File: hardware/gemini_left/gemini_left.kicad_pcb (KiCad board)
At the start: 2 copper layers, 39 parts, among them IC1 XL9555__TSSOP-24_, J1 USB_C_Receptacle_USB2.0_16P, SW1 SW_Push, SW10 SW_Push, SW11 SW_Push, SW12 SW_Push, SW13 SW_Push, SW14 SW_Push, SW15 SW_Push, SW16 SW_Push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

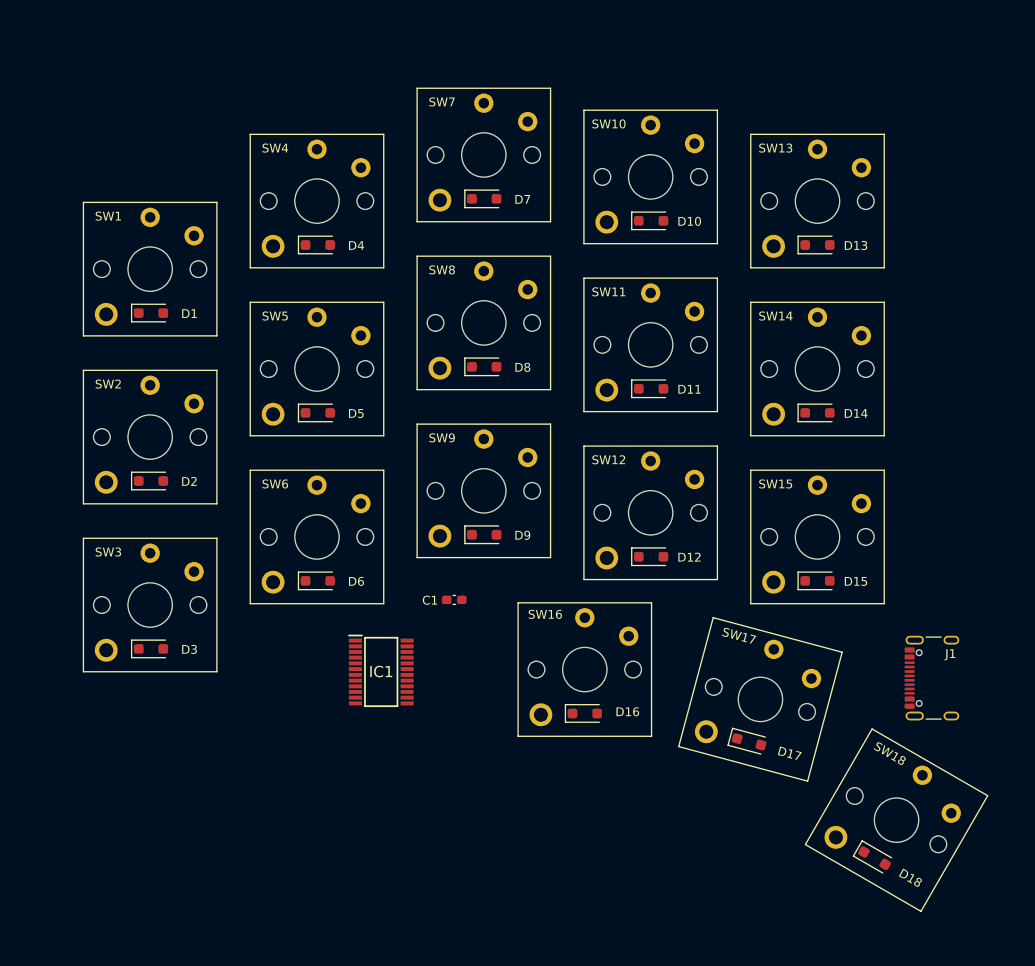
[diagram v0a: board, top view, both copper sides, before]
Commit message: routing of left side & cleanup
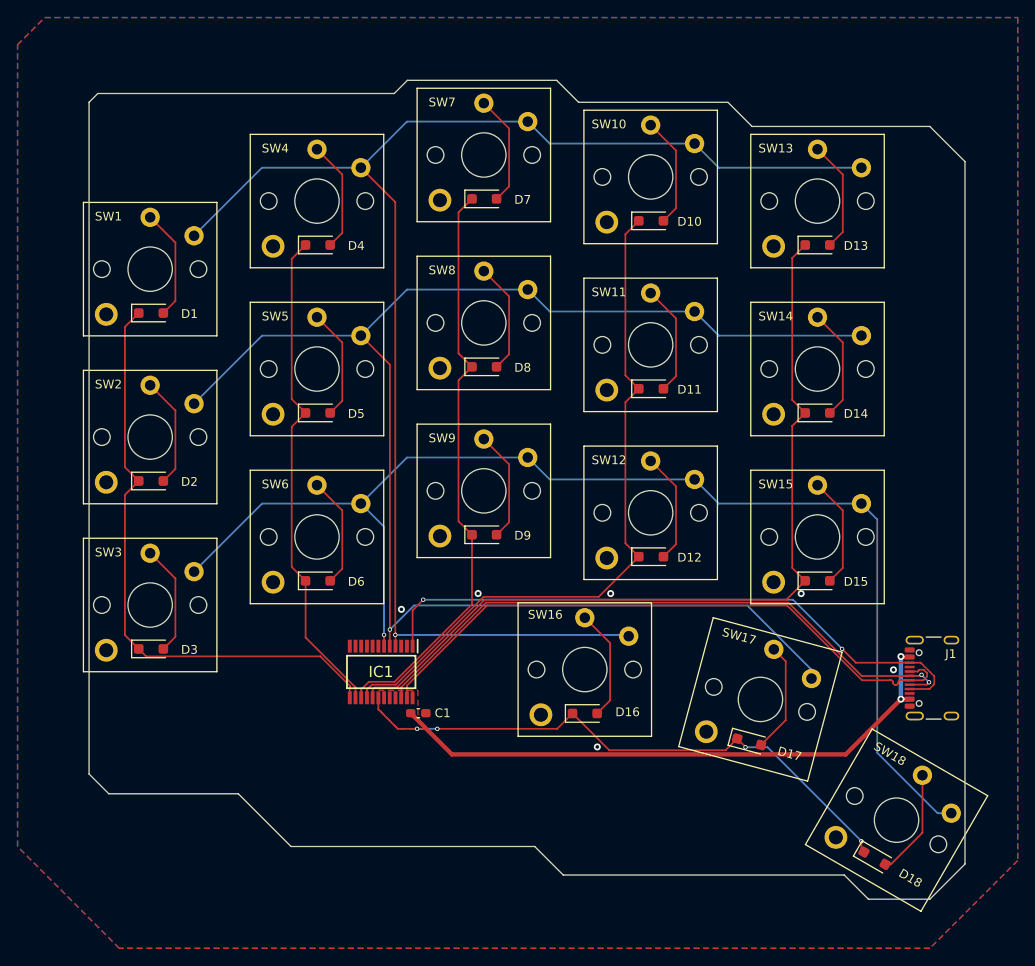
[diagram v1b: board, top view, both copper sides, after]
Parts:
- moved C1 13.5 mm to (220.0, 109.8)
- turned IC1 to -90 degrees
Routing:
- net /LCOL1: track 0.00 -> 173.5 mm, vias 0 -> 1
- net /LCOL0: track 0.00 -> 166.3 mm, vias 0 -> 1
- net /LCOL2: track 0.00 -> 141.3 mm, vias 0 -> 1
- net /LROW4: track 0.00 -> 96.0 mm
- net /LROW3: track 0.00 -> 78.9 mm
- net /DP: track 0.00 -> 71.9 mm
- net /CC: track 0.00 -> 71.5 mm, vias 0 -> 2
- net /DN: track 0.00 -> 71.5 mm, vias 0 -> 2
- net /LROW0: track 0.00 -> 68.0 mm
- net /VBUS: track 0.00 -> 67.9 mm, vias 0 -> 2
- net /LROW5: track 0.00 -> 66.5 mm, vias 0 -> 4
- net /LROW2: track 0.00 -> 66.3 mm
- net /LROW1: track 0.00 -> 56.5 mm
- net Net-(D15-A): track 0.00 -> 12.7 mm
- net Net-(D14-A): track 0.00 -> 12.7 mm
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- added copper zone on F.Cu, net /VBUS
- added copper zone on B.Cu, net GND
- added copper zone on F.Cu, net GND
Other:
- board outline added: 99.7 x 93.2 mm

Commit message: add screw hole
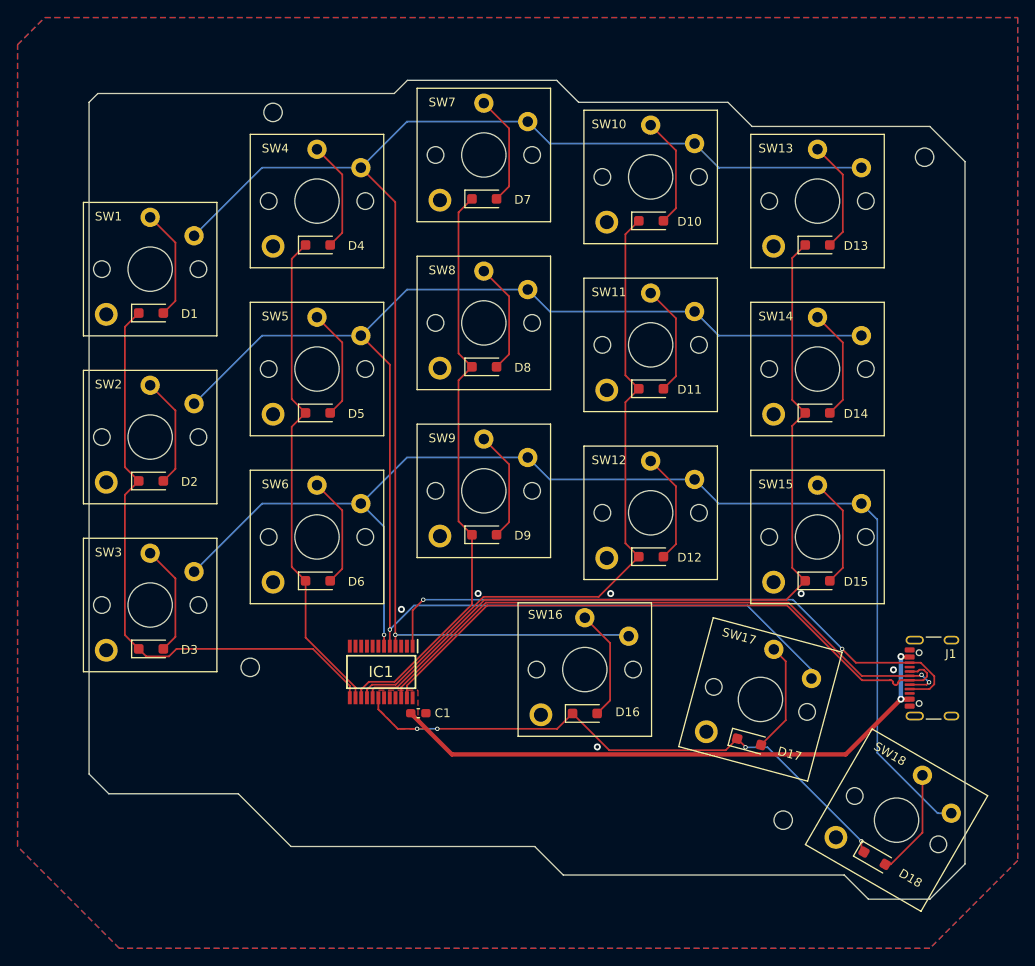
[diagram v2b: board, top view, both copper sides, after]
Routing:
- net /LROW0: track 68.0 -> 68.7 mm
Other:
- outline, holes or cut-outs redrawn

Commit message: update clearance & outline for left side
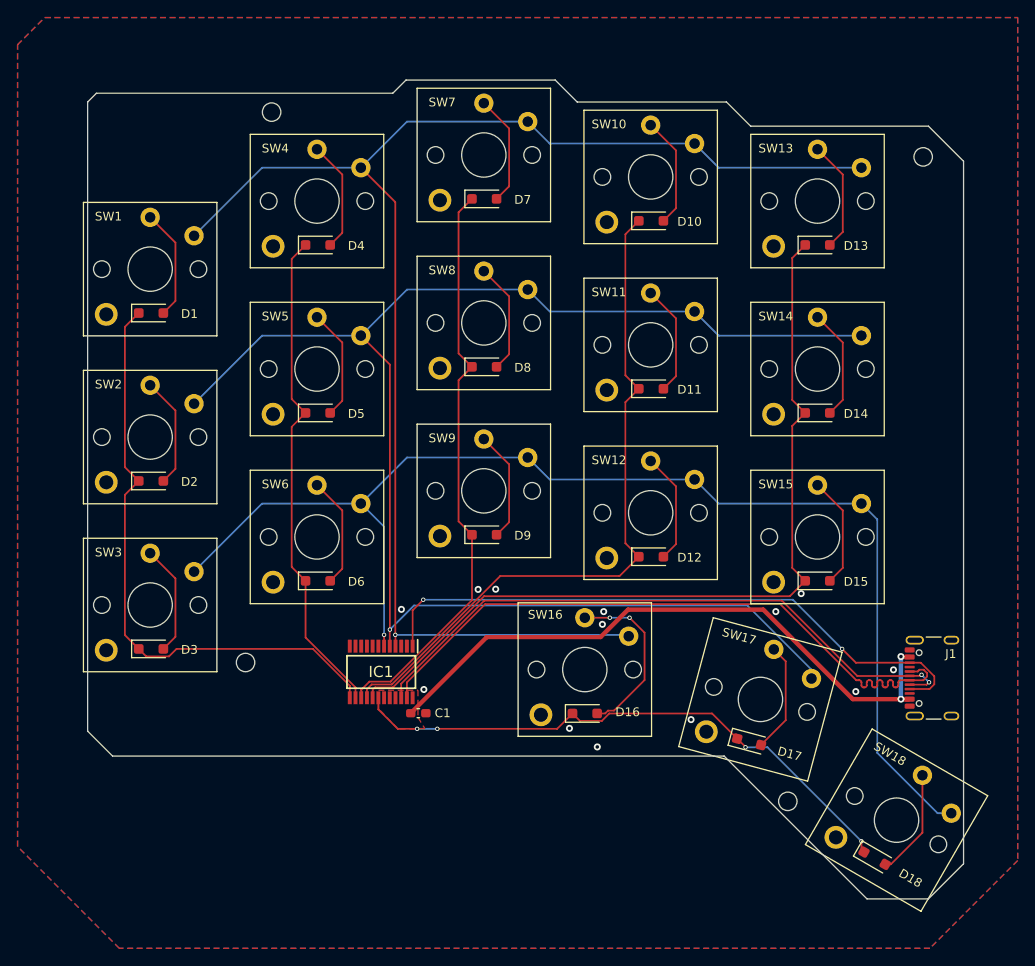
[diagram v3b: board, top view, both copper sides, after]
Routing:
- net Net-(D16-A): track 12.7 -> 19.9 mm, vias 0 -> 2
- net /VBUS: track 67.9 -> 72.5 mm
- net /DP: track 71.9 -> 76.4 mm
- net GND: vias 6 -> 13
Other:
- board size 99.7 x 93.2 mm -> 99.8 x 93.2 mm

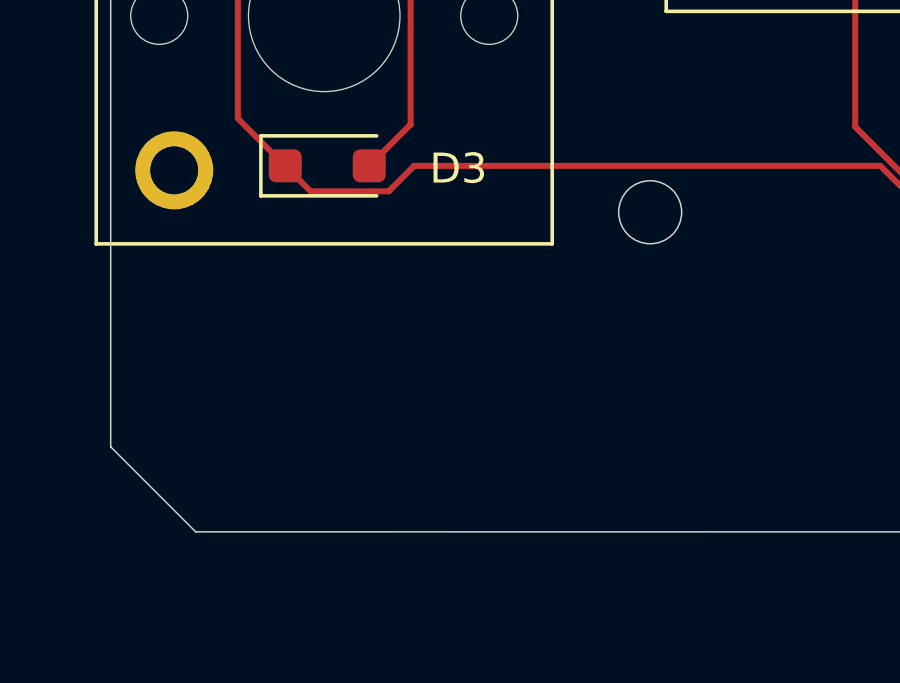
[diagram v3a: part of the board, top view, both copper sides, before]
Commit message: use esp32c3 instead
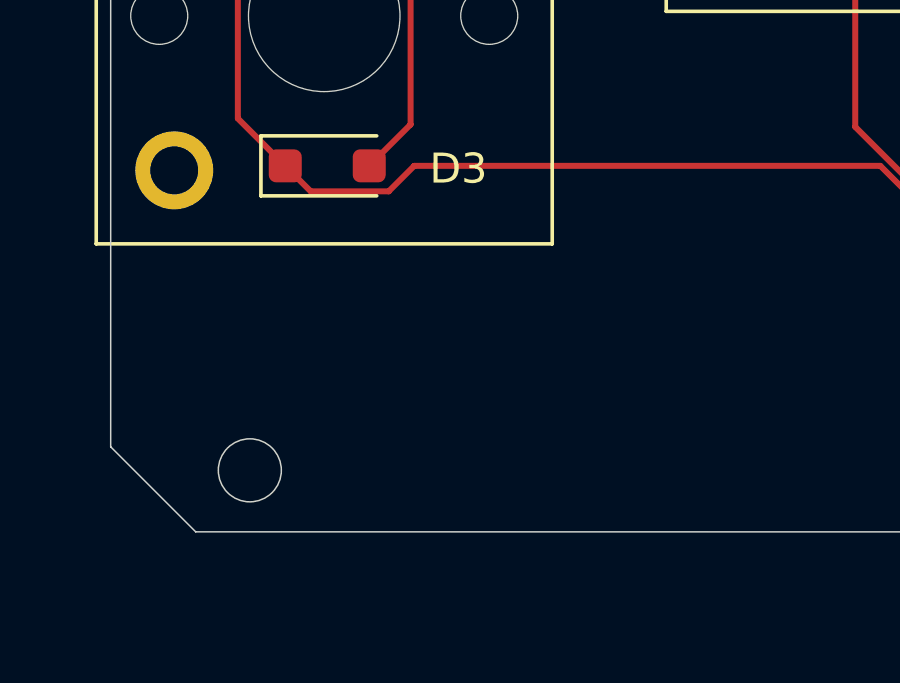
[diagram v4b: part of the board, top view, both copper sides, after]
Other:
- outline, holes or cut-outs redrawn
